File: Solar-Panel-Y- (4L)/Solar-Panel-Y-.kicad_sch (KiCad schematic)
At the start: 59 parts, among them J1 FTS-107-01-X-DV-A, J2 BM02B-SRSS-TB, SW1 D2F-L2-A1, SW2 D2F-L2-A, U1 BQ25570RGRR, U2 OPT3001, U3 MAX40200AUK

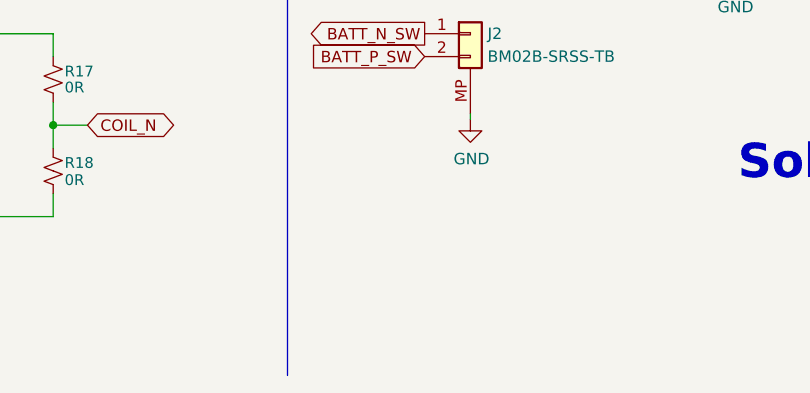
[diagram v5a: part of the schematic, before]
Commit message: Updated Mounting Holes
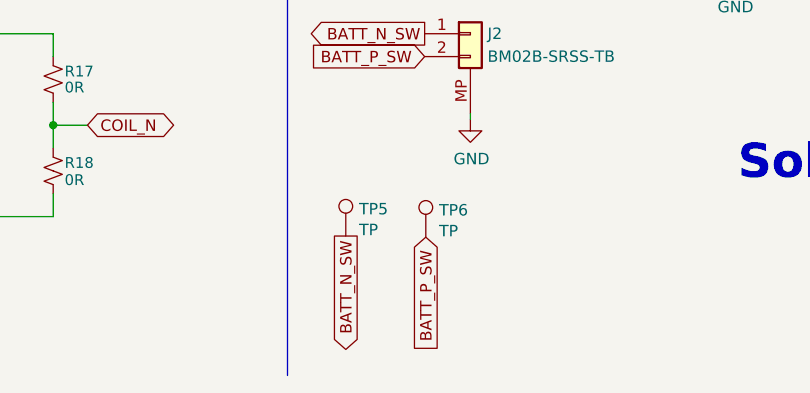
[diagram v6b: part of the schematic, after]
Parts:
- added TP5, TP6: TP, TestPoint:TestPoint_Pad_D1.5mm, symbol Connector:TestPoint
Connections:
- net BATT_N_SW: now also TP5.1
- net BATT_P_SW: now also TP6.1
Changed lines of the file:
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@@
+    )
+  )
+  (global_label "BATT_N_SW" (shape output) (at 215.265 188.468 270) (fields_autoplaced)
+    (effects (font (size 1.27 1.27)) (justify right))
+    (property "Intersheetrefs" "${INTERSHEET_REFS}" (at 215.265 200.94 90)
+      (effects (font (size 1.27 1.27)) (justify right) hide)
     )
   )
@@
     (effects (font (size 1.27 1.27)) (justify right))
     (property "Intersheetrefs" "${INTERSHEET_REFS}" (at 198.6756 133.739 90)
+      (effects (font (size 1.27 1.27)) (justify right) hide)
+    )
+  )
+  (global_label "BATT_P_SW" (shape input) (at 224.155 188.595 270) (fields_autoplaced)
+    (effects (font (size 1.27 1.27)) (justify right))
+    (property "Intersheetrefs" "${INTERSHEET_REFS}" (at 224.155 201.0065 90)
       (effects (font (size 1.27 1.27)) (justify right) hide)
     )
@@
     )
   )
+  (symbol (lib_id "Connector:TestPoint") (at 224.155 188.595 0) (unit 1)
+    (in_bom yes) (on_board yes) (dnp no)
+    (property "Reference" "TP6" (at 225.6282 185.5978 0)
+      (effects (font (size 1.27 1.27)) (justify left))
+    )
+    (property "Value" "TP" (at 225.6282 187.9092 0)
+      (effects (font (size 1.27 1.27)) (justify left))
+    )
+    (property "Footprint" "TestPoint:TestPoint_Pad_D1.5mm" (at 229.235 188.595 0)
+      (effects (font (size 1.27 1.27)) hide)
+    )
+    (property "Datasheet" "~" (at 229.235 188.595 0)
+      (effects (font (size 1.27 1.27)) hide)
+    )
+    (pin "1")
+    (instances
+      (project "Solar-Panel-Y-"
+        (path "/16bd6381-8ac0-4bf2-9dce-ecc20c724b8d"
+          (reference "TP6") (unit 1)
+        )
+      )
+    )
+  )
   (symbol (lib_id "power:GND") (at 229.108 175.514 0) (unit 1)
     (in_bom yes) (on_board yes) (dnp no)
@@
         )
       )
+    )
+  )
+  (symbol (lib_id "Connector:TestPoint") (at 215.265 188.468 0) (unit 1)
+    (in_bom yes) (on_board yes) (dnp no)
+    (property "Reference" "TP5" (at 216.7382 185.4708 0)
+      (effects (font (size 1.27 1.27)) (justify left))
+    )
+    (property "Value" "TP" (at 216.7382 187.7822 0)
+      (effects (font (size 1.27 1.27)) (justify left))
+    )
+    (property "Footprint" "TestPoint:TestPoint_Pad_D1.5mm" (at 220.345 188.468 0)
+      (effects (font (size 1.27 1.27)) hide)
+    )
+    (property "Datasheet" "~" (at 220.345 188.468 0)
+      (effects (font (size 1.27 1.27)) hide)
+    )
+    (pin "1")
+    (instances
+      (project "Solar-Panel-Y-"
+        (path "/16bd6381-8ac0-4bf2-9dce-ecc20c724b8d"
+          (reference "TP5") (unit 1)
+        )
+      )

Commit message: B3/02 Updates
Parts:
- C1: value 1uF -> 0.1uF
- H1, H2, H3, H4: footprint MountingHole:MountingHole_3.2mm_M3_DIN965_Pad -> solarpanels:MountingHole_3.2mm_M3_DIN965_Pad_TopBottom; now left out of the parts list
- TP1, TP2, TP3, TP4, TP5, TP6: now left out of the parts list
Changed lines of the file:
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@@
   (title_block
     (title "PyCubed Mini")
-    (date "2023-02-18")
-    (rev "Rev B3/01")
+    (date "2023-04-12")
+    (rev "Rev B3/02")
     (company "REx Lab Carnegie Mellon University")
     (comment 1 "Z.Manchester")
@@
   )
   (symbol (lib_id "Connector:TestPoint") (at 179.07 126.873 0) (unit 1)
-    (in_bom yes) (on_board yes) (dnp no)
+    (in_bom no) (on_board yes) (dnp no)
     (property "Reference" "TP1" (at 180.5432 123.8758 0)
       (effects (font (size 1.27 1.27)) (justify left))
@@
   )
   (symbol (lib_id "Connector:TestPoint") (at 185.42 126.873 0) (unit 1)
-    (in_bom yes) (on_board yes) (dnp no)
+    (in_bom no) (on_board yes) (dnp no)
     (property "Reference" "TP2" (at 186.8932 123.8758 0)
       (effects (font (size 1.27 1.27)) (justify left))
@@
   )
   (symbol (lib_id "Connector:TestPoint") (at 191.77 126.873 0) (unit 1)
-    (in_bom yes) (on_board yes) (dnp no)
+    (in_bom no) (on_board yes) (dnp no)
     (property "Reference" "TP3" (at 193.2432 123.8758 0)
       (effects (font (size 1.27 1.27)) (justify left))
@@
       (effects (font (size 1.2 1.2)) (justify left))
     )
-    (property "Value" "1uF" (at 27.432 177.546 0)
+    (property "Value" "0.1uF" (at 27.305 177.546 0)
       (effects (font (size 1.2 1.2)) (justify left))
     )
@@
   )
   (symbol (lib_id "Connector:TestPoint") (at 224.155 188.595 0) (unit 1)
-    (in_bom yes) (on_board yes) (dnp no)
+    (in_bom no) (on_board yes) (dnp no)
     (property "Reference" "TP6" (at 225.6282 185.5978 0)
       (effects (font (size 1.27 1.27)) (justify left))
@@
   )
   (symbol (lib_id "Connector:TestPoint") (at 215.265 188.468 0) (unit 1)
-    (in_bom yes) (on_board yes) (dnp no)
+    (in_bom no) (on_board yes) (dnp no)
     (property "Reference" "TP5" (at 216.7382 185.4708 0)
       (effects (font (size 1.27 1.27)) (justify left))
@@
   )
   (symbol (lib_id "Connector:TestPoint") (at 198.755 127 0) (unit 1)
-    (in_bom yes) (on_board yes) (dnp no)
+    (in_bom no) (on_board yes) (dnp no)
     (property "Reference" "TP4" (at 200.2282 124.0028 0)
       (effects (font (size 1.27 1.27)) (justify left))
@@
   )
   (symbol (lib_id "Mechanical:MountingHole_Pad") (at 185.039 92.075 270) (unit 1)
-    (in_bom yes) (on_board yes) (dnp no) (fields_autoplaced)
+    (in_bom no) (on_board yes) (dnp no) (fields_autoplaced)
     (property "Reference" "H1" (at 188.849 91.2403 90)
       (effects (font (size 1.27 1.27)) (justify left))
@@
       (effects (font (size 1.27 1.27)) (justify left))
     )
-    (property "Footprint" "MountingHole:MountingHole_3.2mm_M3_DIN965_Pad" (at 185.039 92.075 0)
+    (property "Footprint" "solarpanels:MountingHole_3.2mm_M3_DIN965_Pad_TopBottom" (at 185.039 92.075 0)
       (effects (font (size 1.27 1.27)) hide)
     )
@@
   )
   (symbol (lib_id "Mechanical:MountingHole_Pad") (at 185.039 104.521 270) (unit 1)
-    (in_bom yes) (on_board yes) (dnp no) (fields_autoplaced)
+    (in_bom no) (on_board yes) (dnp no) (fields_autoplaced)
     (property "Reference" "H3" (at 188.849 103.6863 90)
       (effects (font (size 1.27 1.27)) (justify left))
@@
       (effects (font (size 1.27 1.27)) (justify left))
     )
-    (property "Footprint" "MountingHole:MountingHole_3.2mm_M3_DIN965_Pad" (at 185.039 104.521 0)
+    (property "Footprint" "solarpanels:MountingHole_3.2mm_M3_DIN965_Pad_TopBottom" (at 185.039 104.521 0)
       (effects (font (size 1.27 1.27)) hide)
     )
@@
   )
   (symbol (lib_id "Mechanical:MountingHole_Pad") (at 185.039 98.298 270) (unit 1)
-    (in_bom yes) (on_board yes) (dnp no) (fields_autoplaced)
+    (in_bom no) (on_board yes) (dnp no) (fields_autoplaced)
     (property "Reference" "H2" (at 188.849 97.4633 90)
       (effects (font (size 1.27 1.27)) (justify left))
@@
       (effects (font (size 1.27 1.27)) (justify left))
     )
-    (property "Footprint" "MountingHole:MountingHole_3.2mm_M3_DIN965_Pad" (at 185.039 98.298 0)
+    (property "Footprint" "solarpanels:MountingHole_3.2mm_M3_DIN965_Pad_TopBottom" (at 185.039 98.298 0)
       (effects (font (size 1.27 1.27)) hide)
     )
@@
   )
   (symbol (lib_id "Mechanical:MountingHole_Pad") (at 185.039 110.871 270) (unit 1)
-    (in_bom yes) (on_board yes) (dnp no) (fields_autoplaced)
+    (in_bom no) (on_board yes) (dnp no) (fields_autoplaced)
     (property "Reference" "H4" (at 188.849 110.0363 90)
       (effects (font (size 1.27 1.27)) (justify left))
@@
       (effects (font (size 1.27 1.27)) (justify left))
     )
-    (property "Footprint" "MountingHole:MountingHole_3.2mm_M3_DIN965_Pad" (at 185.039 110.871 0)
+    (property "Footprint" "solarpanels:MountingHole_3.2mm_M3_DIN965_Pad_TopBottom" (at 185.039 110.871 0)
       (effects (font (size 1.27 1.27)) hide)
     )

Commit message: Minor Fixes
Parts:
- renumbered R32 to R31
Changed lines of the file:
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@@
   (symbol (lib_id "Device:R_Small_US") (at 253.365 158.623 90) (unit 1)
     (in_bom yes) (on_board yes) (dnp no)
-    (property "Reference" "R32" (at 253.365 156.591 90)
+    (property "Reference" "R31" (at 253.365 156.591 90)
       (effects (font (size 1.2 1.2)))
     )
@@
       (project "Solar-Panel-Y-"
         (path "/16bd6381-8ac0-4bf2-9dce-ecc20c724b8d"
-          (reference "R32") (unit 1)
+          (reference "R31") (unit 1)
         )
       )
